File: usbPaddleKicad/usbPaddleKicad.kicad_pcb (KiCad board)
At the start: 2 copper layers, 90 x 51 mm, 13 parts, among them U1 RP2040-ZERO, U2 RJ116P4C, U3 RJ116P4C, U4 RJ116P4C, U5 RJ116P4C

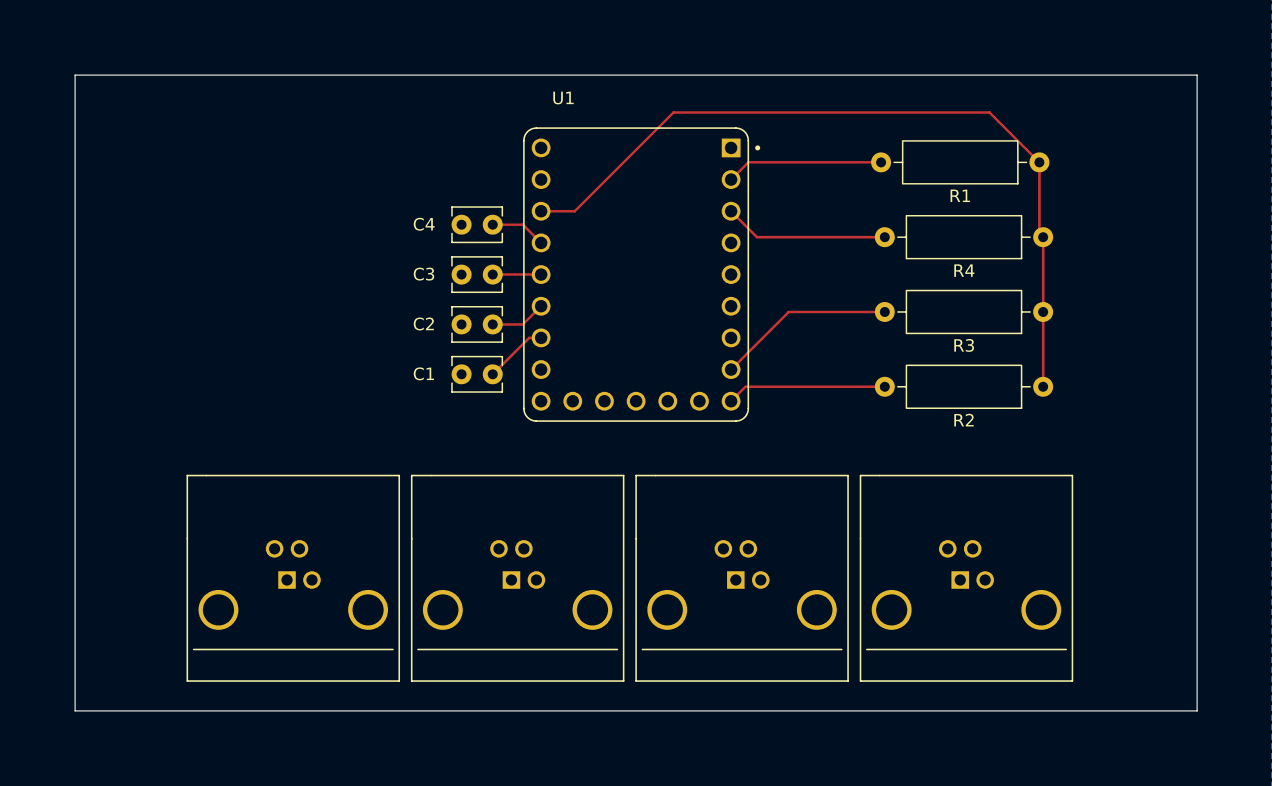
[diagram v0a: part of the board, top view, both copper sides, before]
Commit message: clean up pcb edges and corners
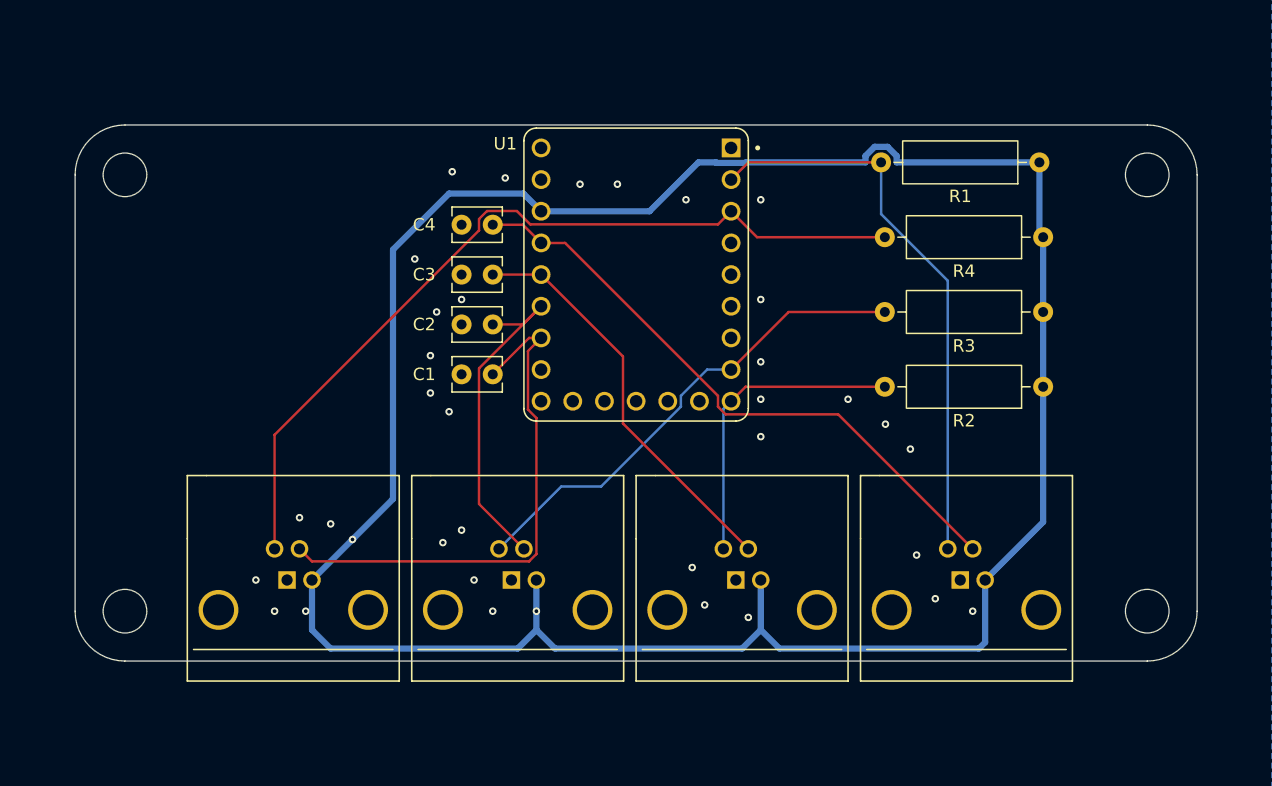
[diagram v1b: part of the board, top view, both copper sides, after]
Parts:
- added ?: , , F.Cu at (95.6, 95.0)
- added ?: , , F.Cu at (177.6, 95.0)
- added ?: , , F.Cu at (95.6, 60.0)
- added ?: , , F.Cu at (177.6, 60.0)
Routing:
- net VCC: track 63.0 -> 196.7 mm, vias 0 -> 3
- net Net-(U1-GP2): track 13.2 -> 67.8 mm
- net Net-(U1-GP29): track 4.48 -> 49.8 mm
- net Net-(U1-GP26): track 5.09 -> 42.8 mm
- net Net-(U1-GP1): track 12.6 -> 45.8 mm
- net Net-(U1-GP28): track 3.88 -> 32.8 mm
- net Net-(U1-GP7): track 14.2 -> 39.3 mm
- net Net-(U1-GP27): track 4.48 -> 27.5 mm
- net Net-(U1-GP8): track 12.8 -> 24.9 mm
- net GND: vias 0 -> 33
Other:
- board size 90 x 51 mm -> 90 x 43 mm

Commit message: add silkscreens
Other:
- board text added: "Paddle Controller Base Unit version 1.0 Dan Shimmyo May 2026"
- board text added: "WayWayWay"
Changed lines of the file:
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@@
 		)
+	)
+	(gr_poly
+		(pts
+			(xy 176.081993 78.320524) (xy 176.081993 77.882854) (xy 177.176165 77.882854) (xy 177.176165 78.320524)
+		)
+		(stroke
+			(width 0)
+			(type solid)
+		)
+		(fill yes)
+		(layer "F.SilkS")
+	)
+	(gr_poly
+		(pts
+			(xy 176.738497 75.256833) (xy 176.738497 74.819172) (xy 176.957331 74.819172) (xy 176.957331 75.256833)
+		)
+		(stroke
+			(width 0)
+			(type solid)
+		)
+		(fill yes)
+		(layer "F.SilkS")
+	)
+	(gr_poly
+		(pts
+			(xy 176.081993 82.916051) (xy 176.081993 82.478385) (xy 176.51966 82.478385) (xy 176.51966 82.69722)
+			(xy 176.738497 82.69722) (xy 176.738497 82.916051)
+		)
+		(stroke
+			(width 0)
+			(type solid)
+		)
+		(fill yes)
+		(layer "F.SilkS")
+	)
+	(gr_poly
+		(pts
+			(xy 176.081993 84.447894) (xy 176.081993 84.010228) (xy 176.51966 84.010228) (xy 176.51966 84.229061)
+			(xy 176.738497 84.229061) (xy 176.738497 84.447894)
+		)
+		(stroke
+			(width 0)
+			(type solid)
+		)
+		(fill yes)
+		(layer "F.SilkS")
+	)
+	(gr_poly
+		(pts
+			(xy 176.081993 85.979736) (xy 176.081993 85.542068) (xy 176.51966 85.542068) (xy 176.51966 85.760903)
+			(xy 176.738497 85.760903) (xy 176.738497 85.979736)
+		)
+		(stroke
+			(width 0)
+			(type solid)
+		)
+		(fill yes)
+		(layer "F.SilkS")
+	)
+	(gr_poly
+		(pts
+			(xy 176.957331 82.916051) (xy 176.957331 82.69722) (xy 176.738497 82.69722) (xy 176.738497 82.478385)
+			(xy 177.176165 82.478385) (xy 177.176165 82.916051)
+		)
+		(stroke
+			(width 0)
+			(type solid)
+		)
+		(fill yes)
+		(layer "F.SilkS")
+	)
+	(gr_poly
+		(pts
+			(xy 176.957331 84.447894) (xy 176.957331 84.229061) (xy 176.738497 84.229061) (xy 176.738497 84.010228)
+			(xy 177.176165 84.010228) (xy 177.176165 84.447894)
+		)
+		(stroke
+			(width 0)
+			(type solid)
+		)
+		(fill yes)
+		(layer "F.SilkS")
+	)
+	(gr_poly
+		(pts
+			(xy 176.957331 85.979735) (xy 176.957331 85.760903) (xy 176.738497 85.760903) (xy 176.738497 85.542068)
+			(xy 177.176165 85.542068) (xy 177.176165 85.979735)
+		)
+		(stroke
+			(width 0)
+			(type solid)
+		)
+		(fill yes)
+		(layer "F.SilkS")
+	)
+	(gr_poly
+		(pts
+			(xy 175.384313 86.941556) (xy 175.384313 67.997472) (xy 177.176164 67.997472) (xy 177.176164 68.472967)
+			(xy 176.738496 68.472967) (xy 176.738496 68.6918) (xy 176.51966 68.6918) (xy 176.51966 69.348308)
+			(xy 176.081993 69.348308) (xy 176.081993 68.91063) (xy 176.300824 68.91063) (xy 176.300824 68.472967)
+			(xy 176.081993 68.472967) (xy 176.081993 68.6918) (xy 175.863155 68.6918) (xy 175.863155 69.567138)
+			(xy 175.863155 70.004811) (xy 175.863155 70.442478) (xy 176.51966 70.442478) (xy 176.51966 70.880153)
+			(xy 175.863155 70.880153) (xy 175.863155 71.317817) (xy 177.176165 71.317817) (xy 177.176165 71.536648)
+			(xy 177.176165 71.755489) (xy 176.081993 71.755489) (xy 176.081993 71.536648) (xy 175.863155 71.536648)
+			(xy 175.863155 72.411992) (xy 175.863155 72.630828) (xy 175.863155 73.068497) (xy 176.738497 73.068497)
+			(xy 176.738497 73.287329) (xy 176.51966 73.287329) (xy 176.51966 73.50616) (xy 176.738497 73.50616)
+			(xy 176.738497 73.725) (xy 175.863155 73.725) (xy 175.863155 74.162666) (xy 176.957331 74.162666)
+			(xy 176.957331 74.3815) (xy 175.863155 74.3815) (xy 175.863155 74.819174) (xy 176.51966 74.819174)
+			(xy 176.51966 75.25684) (xy 175.863155 75.25684) (xy 175.863155 75.694511) (xy 176.300824 75.694511)
+			(xy 176.300824 75.913343) (xy 176.300824 76.132178) (xy 176.081993 76.132178) (xy 176.081993 76.351016)
+			(xy 175.863155 76.351016) (xy 175.863155 76.788681) (xy 176.081993 76.788681) (xy 176.081993 77.007518)
+			(xy 176.300824 77.007518) (xy 176.300824 77.226352) (xy 177.176165 77.226352) (xy 177.176165 77.44519)
+			(xy 176.081993 77.44519) (xy 176.081993 77.66402) (xy 175.863155 77.66402) (xy 175.863155 78.539359)
+			(xy 176.081993 78.539359) (xy 176.081993 78.758194) (xy 176.95733 78.758194) (xy 176.95733 78.977033)
+			(xy 176.95733 79.195866) (xy 176.738496 79.195866) (xy 176.738496 79.414701) (xy 176.51966 79.414701)
+			(xy 176.51966 79.195866) (xy 176.300824 79.195866) (xy 176.300824 78.977033) (xy 175.863155 78.977033)
+			(xy 175.863155 79.414701) (xy 176.300824 79.414701) (xy 176.300824 79.852368) (xy 175.863155 79.852368)
+			(xy 175.863155 80.290039) (xy 176.300825 80.290039) (xy 176.300825 80.071203) (xy 176.51966 80.071203)
+			(xy 176.51966 79.852368) (xy 176.738497 79.852368) (xy 176.738497 80.071203) (xy 176.957331 80.071203)
+			(xy 176.957331 80.290039) (xy 177.176164 80.290039) (xy 177.176164 80.508872) (xy 176.95733 80.508872)
+			(xy 176.95733 80.946547) (xy 177.176164 80.946547) (xy 177.176164 81.384208) (xy 176.738496 81.384208)
+			(xy 176.738496 80.946547) (xy 176.51966 80.946547) (xy 176.51966 81.384208) (xy 176.081993 81.384208)
+			(xy 176.081993 80.946547) (xy 176.300824 80.946547) (xy 176.300824 80.508872) (xy 176.081993 80.508872)
+			(xy 176.081993 80.727707) (xy 175.863155 80.727707) (xy 175.863155 81.603045) (xy 176.081993 81.603045)
+			(xy 176.081993 81.821879) (xy 176.51966 81.821879) (xy 176.51966 81.603045) (xy 176.738497 81.603045)
+			(xy 176.738497 81.821879) (xy 177.176165 81.821879) (xy 177.176165 82.040711) (xy 176.081993 82.040711)
+			(xy 176.081993 82.259552) (xy 175.863155 82.259552) (xy 175.863155 83.134886) (xy 176.081993 83.134886)
+			(xy 176.081993 83.353723) (xy 177.176165 83.353723) (xy 177.176165 83.572556) (xy 176.081993 83.572556)
+			(xy 176.081993 83.791394) (xy 175.863155 83.791394) (xy 175.863155 84.666727) (xy 176.081993 84.666727)
+			(xy 176.081993 84.885566) (xy 177.176165 84.885566) (xy 177.176165 85.104401) (xy 176.081993 85.104401)
+			(xy 176.081993 85.323235) (xy 175.863155 85.323235) (xy 175.863155 86.198574) (xy 176.081993 86.198574)
+			(xy 176.081993 86.41741) (xy 177.176165 86.41741) (xy 177.176165 86.198574) (xy 177.395 86.198574)
+			(xy 177.395 85.323235) (xy 177.176165 85.323235) (xy 177.176165 85.104401) (xy 177.176165 84.885566)
+			(xy 177.176165 84.66673) (xy 177.395 84.66673) (xy 177.395 83.791394) (xy 177.176165 83.791394) (xy 177.176165 83.572556)
+			(xy 177.176165 83.353723) (xy 177.176165 83.134886) (xy 177.395 83.134886) (xy 177.395 82.259552)
+			(xy 177.176165 82.259552) (xy 177.176165 82.040711) (xy 177.176165 81.821879) (xy 177.176165 81.603045)
+			(xy 177.395 81.603045) (xy 177.395 80.727707) (xy 177.176164 80.727707) (xy 177.176164 80.508872)
+			(xy 177.176164 80.290039) (xy 177.395 80.290039) (xy 177.395 79.852368) (xy 176.957331 79.852368)
+			(xy 176.957331 79.414701) (xy 177.395 79.414701) (xy 177.395 78.977033) (xy 176.95733 78.977033)
+			(xy 176.95733 78.758194) (xy 177.176165 78.758194) (xy 177.176165 78.539359) (xy 177.395 78.539359)
+			(xy 177.395 77.66402) (xy 177.176165 77.66402) (xy 177.176165 77.44519) (xy 177.176165 77.226352)
+			(xy 177.395 77.226352) (xy 177.395 76.788681) (xy 176.300824 76.788681) (xy 176.300824 76.351016)
+			(xy 177.395 76.351016) (xy 177.395 75.913343) (xy 176.300824 75.913343) (xy 176.300824 75.694511)
+			(xy 176.957331 75.694511) (xy 176.957331 75.475675) (xy 177.176165 75.475675) (xy 177.176165 75.25684)
+			(xy 177.395 75.25684) (xy 177.395 74.819172) (xy 177.176165 74.819178) (xy 177.176165 74.600337)
+			(xy 176.957331 74.600337) (xy 176.957331 74.3815) (xy 176.957331 74.162666) (xy 177.395 74.162666)
+			(xy 177.395 73.725) (xy 177.176165 73.725) (xy 177.176165 73.50616) (xy 176.957331 73.50616) (xy 176.957331 73.287329)
+			(xy 177.176165 73.287329) (xy 177.176165 73.068497) (xy 177.395 73.068497) (xy 177.395 72.630828)
+			(xy 175.863155 72.630828) (xy 175.863155 72.411992) (xy 176.081993 72.411992) (xy 176.081993 72.193151)
+			(xy 177.176165 72.193151) (xy 177.176165 72.411992) (xy 177.395 72.411992) (xy 177.395 71.536648)
+			(xy 177.176165 71.536648) (xy 177.176165 71.317817) (xy 177.395 71.317817) (xy 177.395 70.880153)
+			(xy 176.738496 70.880153) (xy 176.738496 70.442478) (xy 177.395 70.442478) (xy 177.395 70.004811)
+			(xy 175.863155 70.004811) (xy 175.863155 69.567138) (xy 176.081993 69.567138) (xy 176.081993 69.785971)
+			(xy 176.51966 69.785971) (xy 176.51966 69.567138) (xy 176.738497 69.567138) (xy 176.738497 68.91063)
+			(xy 177.176165 68.91063) (xy 177.176165 69.348308) (xy 176.957331 69.348308) (xy 176.957331 69.785971)
+			(xy 177.176165 69.785971) (xy 177.176165 69.567138) (xy 177.395 69.567138) (xy 177.395 68.6918) (xy 177.176164 68.691799)
+			(xy 177.176164 68.472967) (xy 177.176164 67.997472) (xy 177.885099 67.997472) (xy 177.885099 86.941556)
+		)
+		(stroke
+			(width 0)
+			(type solid)
+		)
+		(fill yes)
+		(layer "F.SilkS")
 	)
 	(gr_arc
@@
 		)
 		(layer "Edge.Cuts")
+	)
+	(gr_text "Paddle Controller Base Unit\nversion 1.0\nDan Shimmyo\nMay 2026"
+		(at 93.395 82.725 0)
+		(layer "F.SilkS")
+		(effects
+			(font
+				(size 1 1)
+				(thickness 0.1)
+			)
+			(justify left bottom)
+		)
+	)
+	(gr_text "WayWayWay"
+		(at 102.395 90.725 0)
+		(layer "B.SilkS")
+		(effects
+			(font
+				(size 1 1)
+				(thickness 0.1)
+			)
+			(justify left bottom mirror)
+		)
 	)
 	(via
@@
 		)
 	)
+	(group ""
+		(members "097f9b12-3ce7-4dd8-80c2-7a7791c8bf5d" "316124bc-566e-4c8b-a785-21bb7c500745"
+			"7052fe72-b55b-4fb8-8955-861fec2543e3" "af0308e3-1c37-4700-bd9d-0899a8ac8868"
+			"b32d9200-aecb-4edc-ac7b-7c54b69891c5" "cf84ed0a-7d3b-4e76-9032-50437a0bbf16"
+			"ebe4eb41-7fbe-4f4f-a397-a3acaf535b1b" "f48a4a30-8c66-487d-acb2-3d6201826b55"
+			"f5174592-8573-410e-8140-6ee038975d77"
+		)
+	)

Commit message: added port numbers
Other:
- board text added: "P1"
- board text added: "P2"
- board text added: "P3"
- board text added: "P4"
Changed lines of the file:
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@@
+		)
+	)
+	(gr_text "P1"
+		(at 108.895 83.225 0)
+		(layer "F.SilkS")
+		(effects
+			(font
+				(size 1.5 1.5)
+				(thickness 0.3)
+				(bold yes)
+			)
+			(justify bottom)
+		)
+	)
+	(gr_text "P2"
+		(at 126.895 83.225 0)
+		(layer "F.SilkS")
+		(effects
+			(font
+				(size 1.5 1.5)
+				(thickness 0.3)
+				(bold yes)
+			)
+			(justify bottom)
+		)
+	)
+	(gr_text "P3"
+		(at 144.895 83.225 0)
+		(layer "F.SilkS")
+		(effects
+			(font
+				(size 1.5 1.5)
+				(thickness 0.3)
+				(bold yes)
+			)
+			(justify bottom)
+		)
+	)
+	(gr_text "P4"
+		(at 162.645 83.225 0)
+		(layer "F.SilkS")
+		(effects
+			(font
+				(size 1.5 1.5)
+				(thickness 0.3)
+				(bold yes)
+			)
+			(justify bottom)
 		)
 	)

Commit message: port numbering in back silkscreen
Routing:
- net VCC: vias 3 -> 2
- net GND: vias 33 -> 34
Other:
- board text added: "BTN"
- board text added: "GND"
- board text added: "POT"
- board text added: "VCC"
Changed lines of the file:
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@@
 		)
 	)
-	(via
-		(at 107.645 94.975)
+	(gr_text "BTN"
+		(at 107.895 88.725 0)
+		(layer "B.SilkS")
+		(effects
+			(font
+				(size 1 1)
+				(thickness 0.1)
+			)
+			(justify left bottom mirror)
+		)
+	)
+	(gr_text "GND"
+		(at 109.645 95.225 0)
+		(layer "B.SilkS")
+		(effects
+			(font
+				(size 1 1)
+				(thickness 0.1)
+			)
+			(justify left bottom mirror)
+		)
+	)
+	(gr_text "POT"
+		(at 111.895 88.725 0)
+		(layer "B.SilkS")
+		(effects
+			(font
+				(size 1 1)
+				(thickness 0.1)
+			)
+			(justify left bottom mirror)
+		)
+	)
+	(gr_text "VCC"
+		(at 113.145 95.225 0)
+		(layer "B.SilkS")
+		(effects
+			(font
+				(size 1 1)
+				(thickness 0.1)
+			)
+			(justify left bottom mirror)
+		)
+	)
+	(gr_text "BTN"
+		(at 125.895 88.725 0)
+		(layer "B.SilkS")
+		(effects
+			(font
+				(size 1 1)
+				(thickness 0.1)
+			)
+			(justify left bottom mirror)
+		)
+	)
+	(gr_text "GND"
+		(at 127.645 95.225 0)
+		(layer "B.SilkS")
+		(effects
+			(font
+				(size 1 1)
+				(thickness 0.1)
+			)
+			(justify left bottom mirror)
+		)
+	)
+	(gr_text "POT"
+		(at 129.895 88.725 0)
+		(layer "B.SilkS")
+		(effects
+			(font
+				(size 1 1)
+				(thickness 0.1)
+			)
+			(justify left bottom mirror)
+		)
+	)
+	(gr_text "VCC"
+		(at 131.145 95.225 0)
+		(layer "B.SilkS")
+		(effects
+			(font
+				(size 1 1)
+				(thickness 0.1)
+			)
+			(justify left bottom mirror)
+		)
+	)
+	(gr_text "BTN"
+		(at 143.895 88.725 0)
+		(layer "B.SilkS")
+		(effects
+			(font
+				(size 1 1)
+				(thickness 0.1)
+			)
+			(justify left bottom mirror)
+		)
+	)
+	(gr_text "GND"
+		(at 145.645 95.225 0)
+		(layer "B.SilkS")
+		(effects
+			(font
+				(size 1 1)
+				(thickness 0.1)
+			)
+			(justify left bottom mirror)
+		)
+	)
+	(gr_text "POT"
+		(at 147.895 88.725 0)
+		(layer "B.SilkS")
+		(effects
+			(font
+				(size 1 1)
+				(thickness 0.1)
+			)
+			(justify left bottom mirror)
+		)
+	)
+	(gr_text "VCC"
+		(at 149.145 95.225 0)
+		(layer "B.SilkS")
+		(effects
+			(font
+				(size 1 1)
+				(thickness 0.1)
+			)
+			(justify left bottom mirror)
+		)
+	)
+	(gr_text "BTN"
+		(at 161.895 88.725 0)
+		(layer "B.SilkS")
+		(effects
+			(font
+				(size 1 1)
+				(thickness 0.1)
+			)
+			(justify left bottom mirror)
+		)
+	)
+	(gr_text "GND"
+		(at 163.645 95.225 0)
+		(layer "B.SilkS")
+		(effects
+			(font
+				(size 1 1)
+				(thickness 0.1)
+			)
+			(justify left bottom mirror)
+		)
+	)
+	(gr_text "POT"
+		(at 165.895 88.725 0)
+		(layer "B.SilkS")
+		(effects
+			(font
+				(size 1 1)
+				(thickness 0.1)
+			)
+			(justify left bottom mirror)
+		)
+	)
+	(gr_text "VCC"
+		(at 167.145 95.225 0)
+		(layer "B.SilkS")
+		(effects
+			(font
+				(size 1 1)
+				(thickness 0.1)
+			)
+			(justify left bottom mirror)
+		)
+	)
+	(via
+		(at 106.395 94.475)
 		(size 0.6)
 		(drill 0.3)
@@
 		(layers "F.Cu" "B.Cu")
 		(free yes)
+		(net "GND")
+	)
+	(via
+		(at 108.395 95.975)
+		(size 0.6)
+		(drill 0.3)
+		(layers "F.Cu" "B.Cu")
 		(net "GND")
 	)
@@
 		(size 0.6)
 		(drill 0.3)
-		(layers "F.Cu" "B.Cu")
-		(net "VCC")
-	)
-	(via
-		(at 110.145 94.975)
-		(size 0.6)
-		(drill 0.3)
